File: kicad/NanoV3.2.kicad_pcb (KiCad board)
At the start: 2 copper layers, 43.2 x 17.8 mm, 24 parts, among them IC2 LM1117IMPX-5.0, IC3 ATMEGA328P-AU, P1 TTL, P2 OUT, P3 INPUT, Q1 s9014, Y1 16MHz

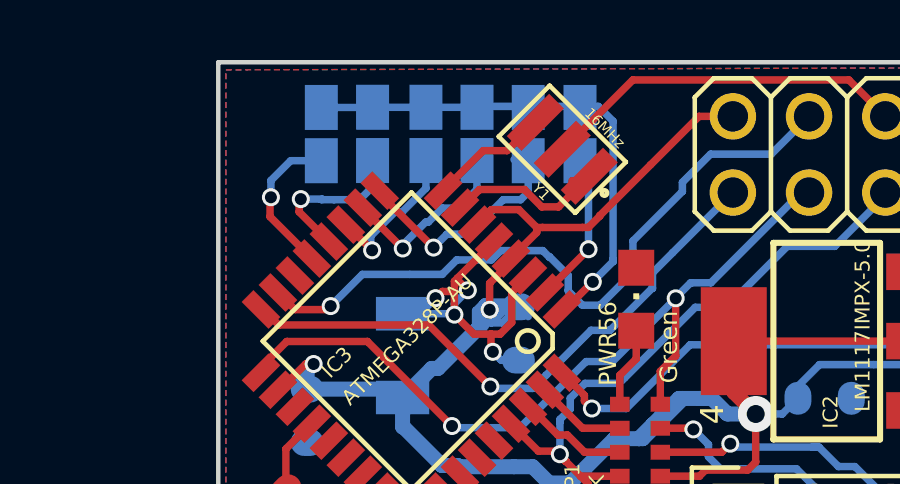
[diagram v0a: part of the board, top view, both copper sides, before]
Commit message: aligned the jumppers
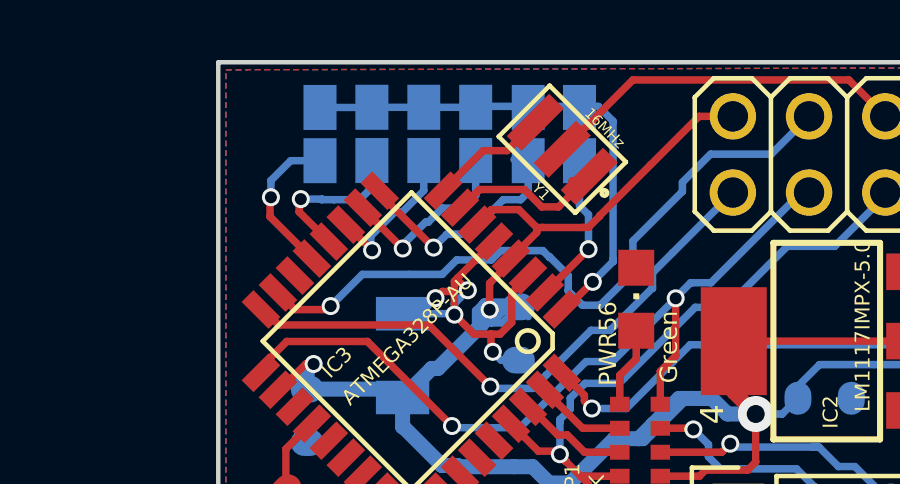
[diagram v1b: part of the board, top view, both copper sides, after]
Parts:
- moved JP4 0.07 mm to (133.8, 98.5)
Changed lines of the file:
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@@
-(kicad_pcb (version 4) (host pcbnew 4.0.2+dfsg1-stable)
+(kicad_pcb (version 4) (host pcbnew 4.0.1-stable)
   (general
     (links 59)
@@
     (thickness 1.6)
     (drawings 91)
-    (tracks 401)
+    (tracks 403)
     (zones 0)
     (modules 24)
@@
     (pad_to_mask_clearance 0.2)
     (aux_axis_origin 127.20828 113.72088)
-    (grid_origin 190.71844 114.01044)
-    (visible_elements 7FFFFFFF)
+    (grid_origin 130.302 101.346)
+    (visible_elements 7FFFF9FF)
     (pcbplotparams
       (layerselection 0x3ffff_80000001)
@@
     (add_net "Net-(P2-Pad1)")
   )
+  (module autoSwitch:SMD-Jummper (layer Bottom)
+    (at 132.032 98.5012 90)
+    (descr CAPACITOR)
+    (tags CAPACITOR)
+    (attr smd)
+    (fp_text reference JP5 (at -2.8448 0 90) (layer B.SilkS)
+      (effects (font (size 0.7 0.7) (thickness 0.1016)) (justify mirror))
+    )
+    (fp_text value ~ (at 2.921 -1.397 90) (layer B.SilkS)
+      (effects (font (size 1.27 1.27) (thickness 0.1016)) (justify mirror))
+    )
+    (fp_line (start -1.47066 0.98298) (end 1.47066 0.98298) (layer Dwgs.User) (width 0.0508))
+    (fp_line (start 1.47066 0.98298) (end 1.47066 -0.98298) (layer Dwgs.User) (width 0.0508))
+    (fp_line (start 1.47066 -0.98298) (end -1.47066 -0.98298) (layer Dwgs.User) (width 0.0508))
+    (fp_line (start -1.47066 -0.98298) (end -1.47066 0.98298) (layer Dwgs.User) (width 0.0508))
+    (pad 1 smd rect (at -0.889 0) (size 1.09982 1.5) (layers Bottom B.Paste B.Mask)
+      (net 20 /D8))
+    (pad 2 smd rect (at 0.88646 0) (size 1.09982 1.5) (layers Bottom B.Paste B.Mask)
+      (net 15 /D3))
+  )
   (module LINEAR_SOT223 (layer Top)
     (at 147.193 105.41 90)
@@
   (module TAN-A (layer Bottom)
     (at 133.05536 107.2896 90)
-    (fp_text reference C5 (at 4.99364 0.08128 90) (layer B.SilkS)
+    (fp_text reference C5 (at 1.8436 1.64664 90) (layer B.SilkS)
       (effects (font (size 0.57912 0.57912) (thickness 0.046329)) (justify left bottom mirror))
     )
@@
     (attr smd)
     (fp_text reference C3 (at -1.016 -1.143 270) (layer B.SilkS)
-      (effects (font (size 0.5 0.5) (thickness 0.1016)) (justify mirror))
-    )
-    (fp_text value 1uF (at 0.508 -1.143 450) (layer B.SilkS)
-      (effects (font (size 0.5 0.5) (thickness 0.1016)) (justify mirror))
+      (effects (font (size 0.5 0.5) (thickness 0.05)) (justify mirror))
+    )
+    (fp_text value 1uF (at 0.508 -1.143 270) (layer B.SilkS)
+      (effects (font (size 0.5 0.5) (thickness 0.05)) (justify mirror))
     )
     (fp_line (start -0.8382 -0.4699) (end -0.33782 -0.4699) (layer Dwgs.User) (width 0.06604))
@@
   )
   (module autoSwitch:SMD-Jummper (layer Bottom)
-    (at 138.96848 98.50628 90)
+    (at 138.952 98.50628 90)
     (descr CAPACITOR)
     (tags CAPACITOR)
     (attr smd)
-    (fp_text reference JP1 (at -2.99212 0.02032 90) (layer B.SilkS)
+    (fp_text reference JP1 (at -2.83972 0.02032 90) (layer B.SilkS)
       (effects (font (size 0.7 0.7) (thickness 0.1016)) (justify mirror))
     )
@@
     (tags CAPACITOR)
     (attr smd)
-    (fp_text reference JP2 (at -2.95148 0.02032 90) (layer B.SilkS)
+    (fp_text reference JP2 (at -2.83972 0.02032 90) (layer B.SilkS)
       (effects (font (size 0.7 0.7) (thickness 0.1016)) (justify mirror))
     )
@@
   )
   (module autoSwitch:SMD-Jummper (layer Bottom)
-    (at 135.5344 98.5012 90)
+    (at 135.492 98.5012 90)
     (descr CAPACITOR)
     (tags CAPACITOR)
     (attr smd)
-    (fp_text reference JP3 (at -2.9972 0.04064 90) (layer B.SilkS)
+    (fp_text reference JP3 (at -2.8448 0.04064 90) (layer B.SilkS)
       (effects (font (size 0.7 0.7) (thickness 0.1016)) (justify mirror))
     )
@@
   )
   (module autoSwitch:SMD-Jummper (layer Bottom)
-    (at 133.8326 98.5012 90)
+    (at 133.762 98.5012 90)
     (descr CAPACITOR)
     (tags CAPACITOR)
     (attr smd)
-    (fp_text reference JP4 (at -2.91592 -0.0254 90) (layer B.SilkS)
+    (fp_text reference JP4 (at -2.8448 0 90) (layer B.SilkS)
       (effects (font (size 0.7 0.7) (thickness 0.1016)) (justify mirror))
     )
@@
   )
   (module autoSwitch:SMD-Jummper (layer Bottom)
-    (at 132.0546 98.5012 90)
+    (at 130.302 98.50628 90)
     (descr CAPACITOR)
     (tags CAPACITOR)
     (attr smd)
-    (fp_text reference JP5 (at -2.83464 -0.01524 90) (layer B.SilkS)
-      (effects (font (size 0.7 0.7) (thickness 0.1016)) (justify mirror))
-    )
-    (fp_text value ~ (at 2.921 -1.397 90) (layer B.SilkS)
-      (effects (font (size 1.27 1.27) (thickness 0.1016)) (justify mirror))
-    )
-    (fp_line (start -1.47066 0.98298) (end 1.47066 0.98298) (layer Dwgs.User) (width 0.0508))
-    (fp_line (start 1.47066 0.98298) (end 1.47066 -0.98298) (layer Dwgs.User) (width 0.0508))
-    (fp_line (start 1.47066 -0.98298) (end -1.47066 -0.98298) (layer Dwgs.User) (width 0.0508))
-    (fp_line (start -1.47066 -0.98298) (end -1.47066 0.98298) (layer Dwgs.User) (width 0.0508))
-    (pad 1 smd rect (at -0.889 0) (size 1.09982 1.5) (layers Bottom B.Paste B.Mask)
-      (net 20 /D8))
-    (pad 2 smd rect (at 0.88646 0) (size 1.09982 1.5) (layers Bottom B.Paste B.Mask)
-      (net 15 /D3))
-  )
-  (module autoSwitch:SMD-Jummper (layer Bottom)
-    (at 130.34772 98.50628 90)
-    (descr CAPACITOR)
-    (tags CAPACITOR)
-    (attr smd)
-    (fp_text reference JP6 (at -2.8702 0.06604 90) (layer B.SilkS)
+    (fp_text reference JP6 (at -2.83972 0 90) (layer B.SilkS)
       (effects (font (size 0.7 0.7) (thickness 0.1016)) (justify mirror))
     )
@@
   (segment (start 135.56488 97.58426) (end 137.24128 97.58426) (width 0.25) (layer Bottom) (net 15))
   (segment (start 137.24128 97.58426) (end 138.96848 97.58426) (width 0.25) (layer Bottom) (net 15))
-  (segment (start 139.25296 99.71532) (end 139.25296 102.34676) (width 0.25) (layer Bottom) (net 16))
+  (segment (start 139.25296 101.19696) (end 138.952 100.896) (width 0.25) (layer Bottom) (net 16))
+  (segment (start 138.952 100.896) (end 138.952 99.39528) (width 0.25) (layer Bottom) (net 16))
+  (segment (start 139.25296 102.34676) (end 139.25296 101.19696) (width 0.25) (layer Bottom) (net 16))
   (segment (start 139.25296 102.34676) (end 137.810833 103.788887) (width 0.25) (layer Top) (net 16))
   (via (at 139.25296 102.34676) (size 0.6) (drill 0.4) (layers Top Bottom) (net 16))
@@
   (segment (start 137.24128 99.35972) (end 136.76884 99.35972) (width 0.25) (layer Bottom) (net 17))
   (segment (start 133.06044 102.32136) (end 133.06044 102.20452) (width 0.25) (layer Bottom) (net 18))
+  (segment (start 133.91388 101.44252) (end 134.38124 100.97516) (width 0.25) (layer Bottom) (net 18))
+  (segment (start 135.07284 100.97516) (end 135.492 100.556) (width 0.25) (layer Bottom) (net 18))
   (segment (start 133.06044 102.20452) (end 133.82244 101.44252) (width 0.25) (layer Bottom) (net 18))
   (segment (start 133.82244 101.44252) (end 133.91388 101.44252) (width 0.25) (layer Bottom) (net 18))
-  (segment (start 135.5344 100.35032) (end 135.5344 99.3902) (width 0.25) (layer Bottom) (net 18))
-  (segment (start 134.90956 100.97516) (end 135.5344 100.35032) (width 0.25) (layer Bottom) (net 18))
-  (segment (start 134.38124 100.97516) (end 134.90956 100.97516) (width 0.25) (layer Bottom) (net 18))
-  (segment (start 133.91388 101.44252) (end 134.38124 100.97516) (width 0.25) (layer Bottom) (net 18))
+  (segment (start 134.38124 100.97516) (end 135.07284 100.97516) (width 0.25) (layer Bottom) (net 18))
+  (segment (start 135.492 100.556) (end 135.492 99.3902) (width 0.25) (layer Bottom) (net 18))
   (segment (start 135.5344 99.3902) (end 135.5344 99.42068) (width 0.25) (layer Bottom) (net 18))
   (segment (start 133.06044 102.32136) (end 131.728887 100.989807) (width 0.25) (layer Top) (net 18))
   (via (at 133.06044 102.32136) (size 0.6) (drill 0.4) (layers Top Bottom) (net 18))
   (segment (start 131.728887 100.989807) (end 131.728887 100.96046) (width 0.25) (layer Top) (net 18))
+  (segment (start 133.01472 101.10724) (end 133.04496 101.10724) (width 0.25) (layer Bottom) (net 19))
+  (segment (start 133.04496 101.10724) (end 133.762 100.3902) (width 0.25) (layer Bottom) (net 19))
+  (segment (start 133.762 100.3902) (end 133.762 99.3902) (width 0.25) (layer Bottom) (net 19))
   (segment (start 133.01472 101.10724) (end 133.04012 101.10724) (width 0.25) (layer Bottom) (net 19))
-  (segment (start 133.04012 101.10724) (end 133.8326 100.31476) (width 0.25) (layer Bottom) (net 19))
   (segment (start 132.85216 101.10724) (end 132.79628 101.10724) (width 0.25) (layer Bottom) (net 19))
   (segment (start 132.79628 101.10724) (end 131.99364 101.90988) (width 0.25) (layer Bottom) (net 19))
   (segment (start 132.85216 101.10724) (end 133.01472 101.10724) (width 0.25) (layer Bottom) (net 19))
-  (segment (start 133.8326 100.31476) (end 133.8326 99.3902) (width 0.25) (layer Bottom) (net 19))
   (segment (start 133.8326 99.3902) (end 133.8326 99.7966) (width 0.25) (layer Bottom) (net 19))
   (segment (start 131.99364 102.3366) (end 132.03936 102.38232) (width 0.25) (layer Bottom) (net 19))
@@
   (segment (start 130.3528 100.69576) (end 130.76936 100.69576) (width 0.25) (layer Bottom) (net 20))
   (segment (start 132.0546 99.41052) (end 132.0546 99.3902) (width 0.25) (layer Bottom) (net 20))
-  (segment (start 132.0546 99.3902) (end 131.65836 99.3902) (width 0.25) (layer Bottom) (net 20))
   (segment (start 130.3528 100.69576) (end 130.37312 100.67544) (width 0.25) (layer Bottom) (net 20))
   (segment (start 130.37312 100.67544) (end 129.66192 100.67544) (width 0.25) (layer Bottom) (net 20))

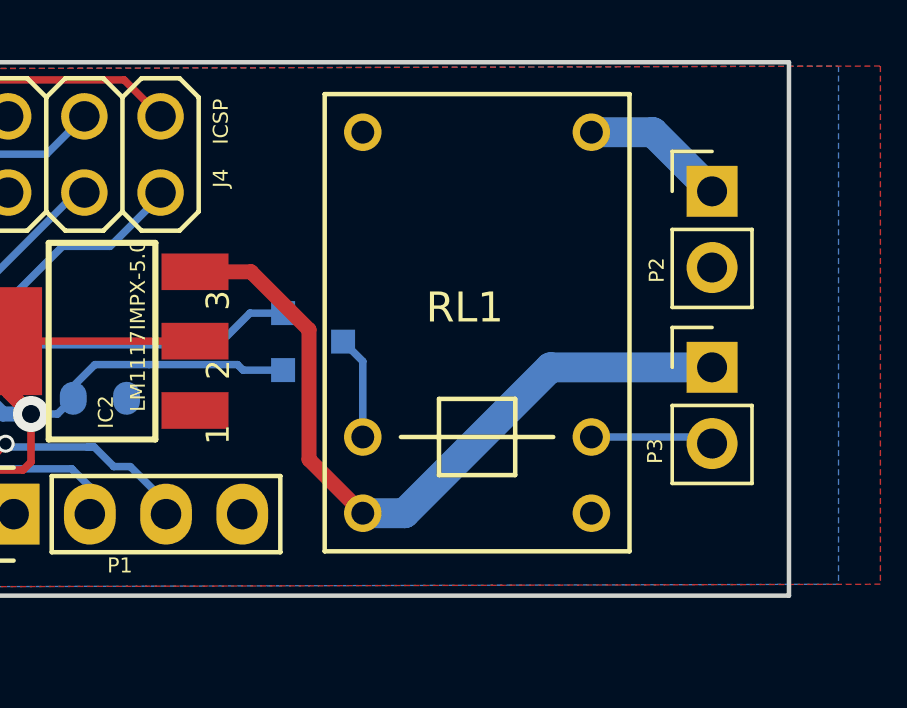
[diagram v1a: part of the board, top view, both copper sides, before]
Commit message: fixed a footprint error for HK4001 relay
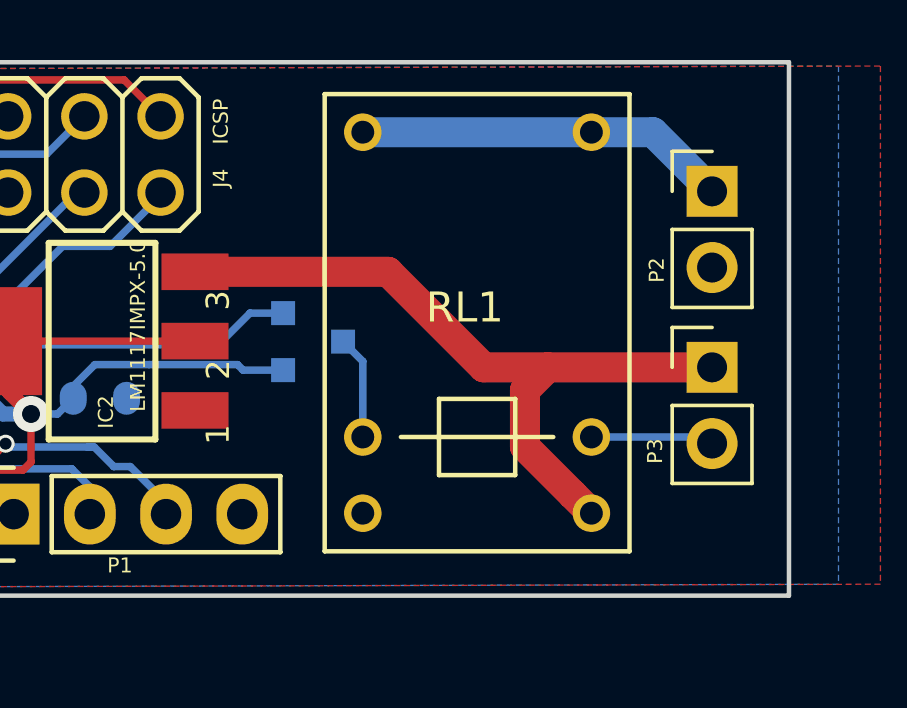
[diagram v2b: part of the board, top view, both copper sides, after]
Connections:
- IC3 pad 14: (no net) -> /D10
- IC3 pad 19: (no net) -> /A6
- IC3 pad 22: (no net) -> /A7
- IC3 pad 23: (no net) -> /A0
- IC3 pad 24: (no net) -> /A1
- IC3 pad 25: (no net) -> /A2
- IC3 pad 26: (no net) -> /A3
- IC3 pad 27: (no net) -> /A4
- IC3 pad 28: (no net) -> /A5
- RL1 pad 10: (no net) -> Net-(P2-Pad1)
- RL1 pad 12: VIN -> Net-(RL1-Pad12)
- RL1 pad 14: (no net) -> VIN
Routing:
- net Net-(P2-Pad1): track 10.4 -> 18.0 mm
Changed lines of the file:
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@@
 (kicad_pcb (version 4) (host pcbnew 4.0.1-stable)
   (general
-    (links 59)
+    (links 60)
     (no_connects 1)
     (area 126.836099 96.038599 170.166101 113.968601)
     (thickness 1.6)
     (drawings 91)
-    (tracks 403)
+    (tracks 405)
     (zones 0)
     (modules 24)
-    (nets 27)
+    (nets 37)
   )
   (page A4)
@@
     (aux_axis_origin 127.20828 113.72088)
     (grid_origin 130.302 101.346)
-    (visible_elements 7FFFF9FF)
+    (visible_elements 7FFFFFFF)
     (pcbplotparams
       (layerselection 0x3ffff_80000001)
@@
   (net 25 "Net-(C2-Pad2)")
   (net 26 /RX)
+  (net 27 /D10)
+  (net 28 /A6)
+  (net 29 /A7)
+  (net 30 /A0)
+  (net 31 /A1)
+  (net 32 /A2)
+  (net 33 /A3)
+  (net 34 /A4)
+  (net 35 /A5)
+  (net 36 "Net-(RL1-Pad12)")
   (net_class Default "This is the default net class."
     (clearance 0.2)
@@
     (uvia_drill 0.1)
     (add_net +5V)
+    (add_net /A0)
+    (add_net /A1)
+    (add_net /A2)
+    (add_net /A3)
+    (add_net /A4)
+    (add_net /A5)
+    (add_net /A6)
+    (add_net /A7)
     (add_net /AREF)
     (add_net /D0/RX)
     (add_net /D1/TX)
+    (add_net /D10)
     (add_net /D11/MOSI)
     (add_net /D12/MISO)
@@
     (add_net "Net-(C2-Pad2)")
     (add_net "Net-(Q1-Pad3)")
+    (add_net "Net-(RL1-Pad12)")
   )
   (net_class w0.5 ""
@@
     (uvia_dia 0.4)
     (uvia_drill 0.2)
-    (add_net VIN)
   )
   (net_class w1.0 ""
@@
     (uvia_drill 0.4)
     (add_net "Net-(P2-Pad1)")
+    (add_net VIN)
   )
   (module autoSwitch:SMD-Jummper (layer Bottom)
@@
     (pad 13 smd rect (at 0.4 4.2926 225) (size 0.5588 1.27) (layers Top F.Paste F.Mask)
       (net 21 /D9))
-    (pad 14 smd rect (at 1.2 4.2926 225) (size 0.5588 1.27) (layers Top F.Paste F.Mask))
+    (pad 14 smd rect (at 1.2 4.2926 225) (size 0.5588 1.27) (layers Top F.Paste F.Mask)
+      (net 27 /D10))
     (pad 15 smd rect (at 2 4.2926 225) (size 0.5588 1.27) (layers Top F.Paste F.Mask)
       (net 8 /D11/MOSI))
@@
     (pad 18 smd rect (at 4.2926 2 225) (size 1.27 0.5588) (layers Top F.Paste F.Mask)
       (net 2 +5V))
-    (pad 19 smd rect (at 4.2926 1.2 225) (size 1.27 0.5588) (layers Top F.Paste F.Mask))
+    (pad 19 smd rect (at 4.2926 1.2 225) (size 1.27 0.5588) (layers Top F.Paste F.Mask)
+      (net 28 /A6))
     (pad 20 smd rect (at 4.2926 0.4 225) (size 1.27 0.5588) (layers Top F.Paste F.Mask)
       (net 3 /AREF))
     (pad 21 smd rect (at 4.2926 -0.4 225) (size 1.27 0.5588) (layers Top F.Paste F.Mask)
       (net 1 COM))
-    (pad 22 smd rect (at 4.2926 -1.2 225) (size 1.27 0.5588) (layers Top F.Paste F.Mask))
-    (pad 23 smd rect (at 4.2926 -2 225) (size 1.27 0.5588) (layers Top F.Paste F.Mask))
-    (pad 24 smd rect (at 4.2926 -2.8 225) (size 1.27 0.5588) (layers Top F.Paste F.Mask))
-    (pad 25 smd rect (at 2.8 -4.2926 225) (size 0.5588 1.27) (layers Top F.Paste F.Mask))
-    (pad 26 smd rect (at 2 -4.2926 225) (size 0.5588 1.27) (layers Top F.Paste F.Mask))
-    (pad 27 smd rect (at 1.2 -4.2926 225) (size 0.5588 1.27) (layers Top F.Paste F.Mask))
-    (pad 28 smd rect (at 0.4 -4.2926 225) (size 0.5588 1.27) (layers Top F.Paste F.Mask))
+    (pad 22 smd rect (at 4.2926 -1.2 225) (size 1.27 0.5588) (layers Top F.Paste F.Mask)
+      (net 29 /A7))
+    (pad 23 smd rect (at 4.2926 -2 225) (size 1.27 0.5588) (layers Top F.Paste F.Mask)
+      (net 30 /A0))
+    (pad 24 smd rect (at 4.2926 -2.8 225) (size 1.27 0.5588) (layers Top F.Paste F.Mask)
+      (net 31 /A1))
+    (pad 25 smd rect (at 2.8 -4.2926 225) (size 0.5588 1.27) (layers Top F.Paste F.Mask)
+      (net 32 /A2))
+    (pad 26 smd rect (at 2 -4.2926 225) (size 0.5588 1.27) (layers Top F.Paste F.Mask)
+      (net 33 /A3))
+    (pad 27 smd rect (at 1.2 -4.2926 225) (size 0.5588 1.27) (layers Top F.Paste F.Mask)
+      (net 34 /A4))
+    (pad 28 smd rect (at 0.4 -4.2926 225) (size 0.5588 1.27) (layers Top F.Paste F.Mask)
+      (net 35 /A5))
     (pad 29 smd rect (at -0.4 -4.2926 225) (size 0.5588 1.27) (layers Top F.Paste F.Mask)
       (net 4 /RESET))
@@
       (net 1 COM))
     (pad 12 thru_hole circle (at 0 -7.62 90) (size 1.25 1.25) (drill 0.762) (layers *.Cu *.Mask)
+      (net 36 "Net-(RL1-Pad12)"))
+    (pad 14 thru_hole circle (at 0 0 90) (size 1.25 1.25) (drill 0.762) (layers *.Cu *.Mask)
       (net 14 VIN))
-    (pad 14 thru_hole circle (at 0 0 90) (size 1.25 1.25) (drill 0.762) (layers *.Cu *.Mask))
     (pad A1 thru_hole circle (at 2.54 -7.62 90) (size 1.25 1.25) (drill 0.762) (layers *.Cu *.Mask)
       (net 24 "Net-(Q1-Pad3)"))
-    (pad 10 thru_hole circle (at 12.7 -7.62 90) (size 1.25 1.25) (drill 0.762) (layers *.Cu *.Mask F.SilkS))
+    (pad 10 thru_hole circle (at 12.7 -7.62 90) (size 1.25 1.25) (drill 0.762) (layers *.Cu *.Mask F.SilkS)
+      (net 23 "Net-(P2-Pad1)"))
     (model ${KISYS3DMOD}/Relays_THT.3dshapes/Relay_SPDT_OMRON-G5LE-1.wrl
       (at (xyz 0 0 0))
@@
   (segment (start 140.843 105.99928) (end 140.295 106.54728) (width 0.25) (layer Top) (net 13))
   (segment (start 140.97 105.19) (end 140.843 105.063) (width 0.25) (layer Top) (net 13))
-  (segment (start 150.2918 103.0986) (end 152.16124 103.0986) (width 0.5) (layer Top) (net 14))
-  (segment (start 154.09164 109.35208) (end 155.88488 111.14532) (width 0.5) (layer Top) (net 14))
-  (segment (start 154.09164 105.029) (end 154.09164 109.35208) (width 0.5) (layer Top) (net 14))
-  (segment (start 152.16124 103.0986) (end 154.09164 105.029) (width 0.5) (layer Top) (net 14))
-  (segment (start 155.88488 111.14532) (end 157.2768 111.14532) (width 1) (layer Bottom) (net 14))
-  (segment (start 157.2768 111.14532) (end 162.13836 106.28376) (width 1) (layer Bottom) (net 14))
-  (segment (start 162.13836 106.28376) (end 167.52824 106.28376) (width 1) (layer Bottom) (net 14))
+  (segment (start 162.052 106.28376) (end 159.91376 106.28376) (width 1) (layer Top) (net 14))
+  (segment (start 167.52824 106.28376) (end 162.052 106.28376) (width 1) (layer Top) (net 14))
+  (segment (start 162.052 106.28376) (end 161.29 107.04576) (width 1) (layer Top) (net 14))
+  (segment (start 161.29 107.04576) (end 161.29 108.93044) (width 1) (layer Top) (net 14))
+  (segment (start 161.29 108.93044) (end 162.879881 110.520321) (width 1) (layer Top) (net 14))
+  (segment (start 162.879881 110.520321) (end 163.50488 111.14532) (width 1) (layer Top) (net 14))
+  (segment (start 159.91376 106.28376) (end 156.7286 103.0986) (width 1) (layer Top) (net 14))
+  (segment (start 156.7286 103.0986) (end 150.2918 103.0986) (width 1) (layer Top) (net 14))
   (segment (start 140.07084 98.07956) (end 140.07084 102.75824) (width 0.25) (layer Bottom) (net 15))
   (segment (start 140.07084 102.75824) (end 140.07084 102.68712) (width 0.25) (layer Bottom) (net 15))
@@
   (segment (start 138.365226 106.465428) (end 138.365226 106.569506) (width 0.25) (layer Top) (net 22))
   (segment (start 138.365226 106.544106) (end 138.365226 106.465428) (width 0.25) (layer Top) (net 22))
+  (segment (start 163.50488 98.44532) (end 155.88488 98.44532) (width 1) (layer Bottom) (net 23))
   (segment (start 163.50488 98.44532) (end 165.5572 98.44532) (width 1) (layer Bottom) (net 23))
   (segment (start 165.5572 98.44532) (end 167.52824 100.41636) (width 1) (layer Bottom) (net 23))
